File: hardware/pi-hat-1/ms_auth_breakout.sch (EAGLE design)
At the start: 37 parts, among them IC1 ULN2003AD, J11 BUCK_MODULEHORIZONTAL, J9 POWER_JACKPTH_LOCK, Q1 DMN3023L, Q2 DMN3023L, Q3 DMN3023L, Q4 DMN3023L, Q5 DMN3023L, Q6 DMN3023L

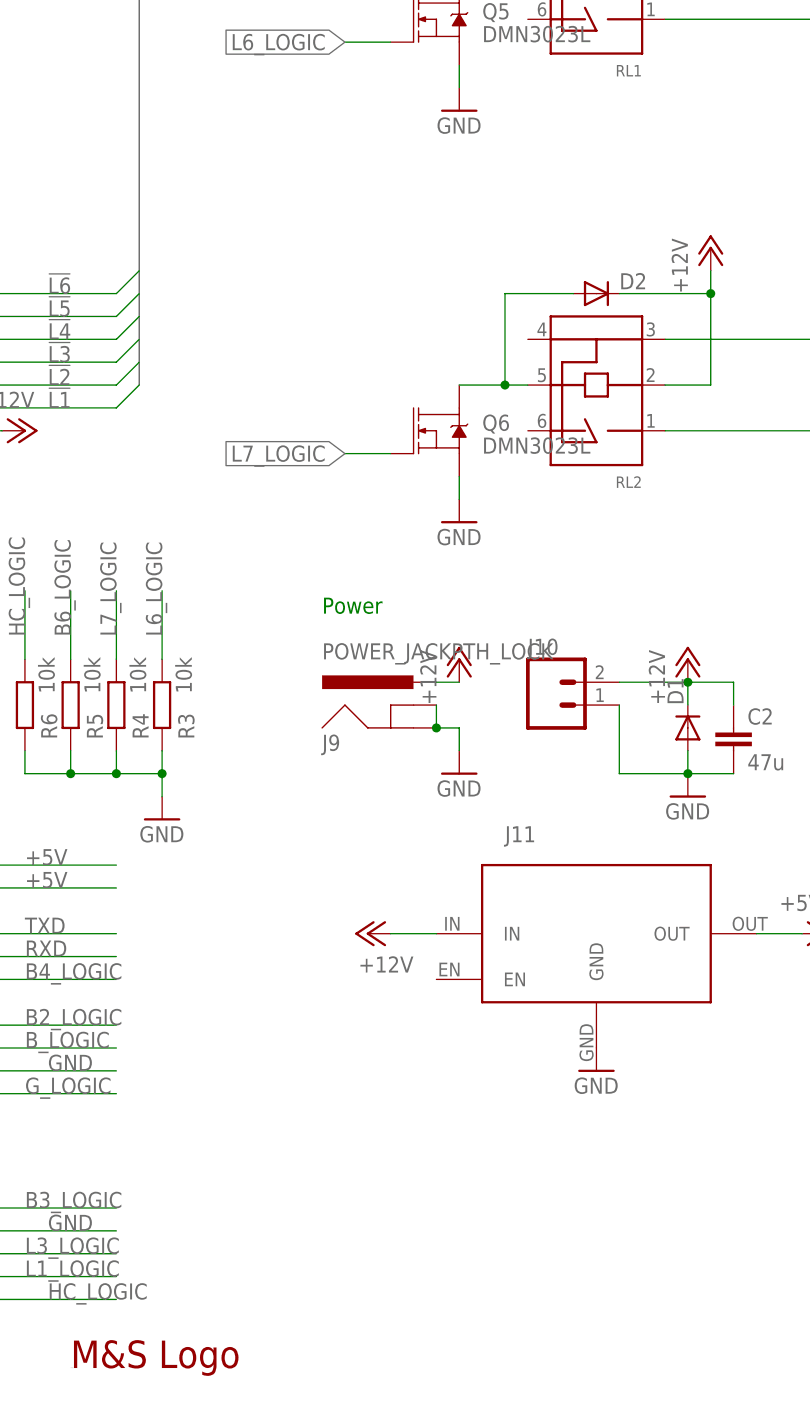
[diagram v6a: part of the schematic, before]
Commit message: Add relay MPN, OSH Certification mark
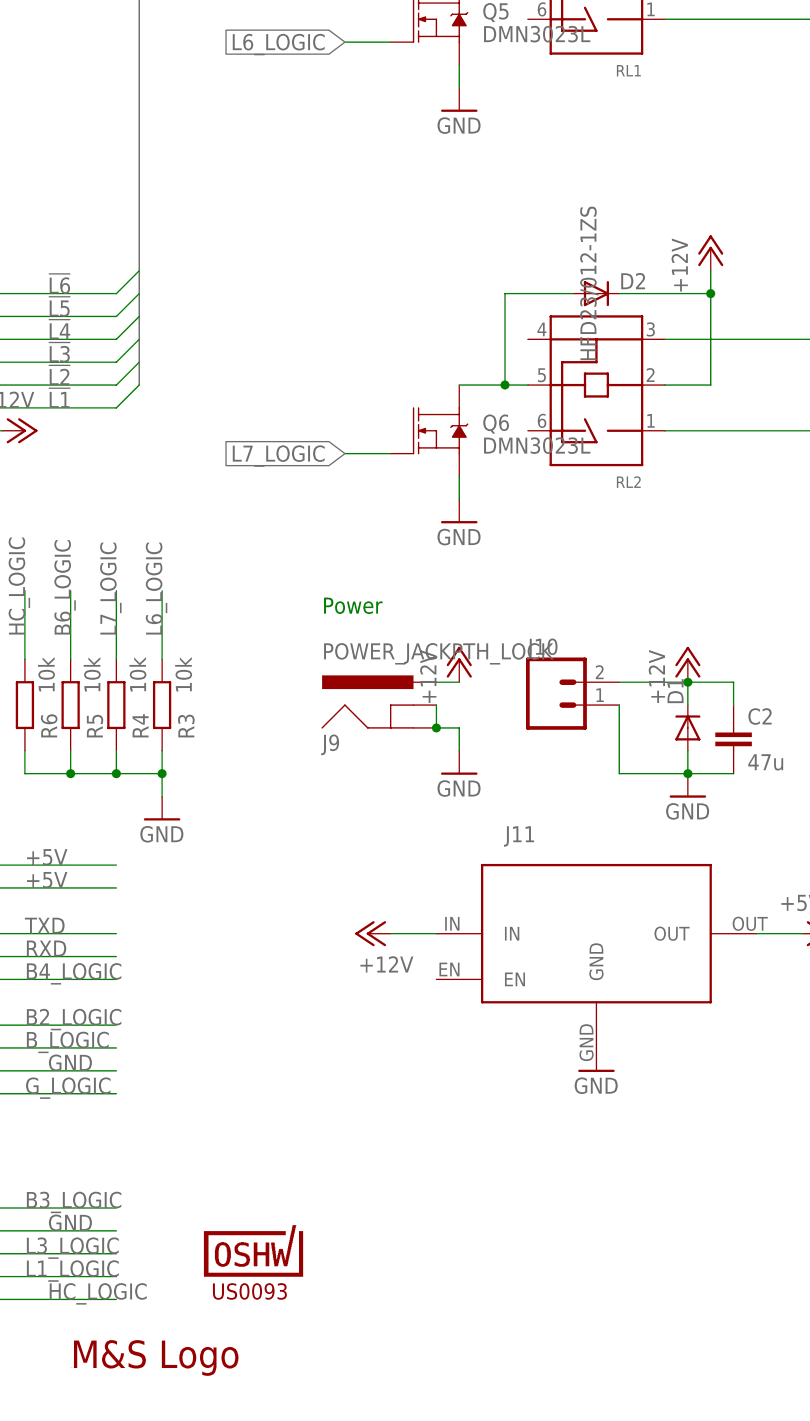
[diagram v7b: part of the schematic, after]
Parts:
- added U$2: US0093, OSHWA:CERT-SMALL
- RL1, RL2: MFN (none) -> HF; MPN (none) -> HFD23/012-1ZS
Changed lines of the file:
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@@
 <part name="Q5" library="SparkFun-DiscreteSemi" deviceset="MOSFET-NCH" device="-AO3404A" value="DMN3023L"/>
 <part name="Q6" library="SparkFun-DiscreteSemi" deviceset="MOSFET-NCH" device="-AO3404A" value="DMN3023L"/>
-<part name="RL1" library="hfd23" deviceset="HFD23_SPDT" device=""/>
-<part name="RL2" library="hfd23" deviceset="HFD23_SPDT" device=""/>
+<part name="RL1" library="hfd23" deviceset="HFD23_SPDT" device="">
+<attribute name="MFN" value="HF"/>
+<attribute name="MPN" value="HFD23/012-1ZS"/>
+</part>
+<part name="RL2" library="hfd23" deviceset="HFD23_SPDT" device="">
+<attribute name="MFN" value="HF"/>
+<attribute name="MPN" value="HFD23/012-1ZS"/>
+</part>
 <part name="GND9" library="supply1" deviceset="GND" device=""/>
 <part name="GND14" library="supply1" deviceset="GND" device=""/>
@@
 <part name="R6" library="Tim-Pretty" deviceset="R-EU_" device="R0805" value="10k"/>
 <part name="J5" library="SparkFun-Connectors" deviceset="CONN_06" device="POLAR_LOCK"/>
+<part name="U$2" library="OSHWA" deviceset="CERT" device="-SMALL" value="US0093"/>
 </parts>
 <sheets>
@@
 <instance part="Q5" gate="NMOS" x="157.48" y="157.48"/>
 <instance part="Q6" gate="NMOS" x="157.48" y="111.76"/>
-<instance part="RL1" gate="G$1" x="175.26" y="165.1" rot="R90"/>
-<instance part="RL2" gate="G$1" x="175.26" y="119.38" rot="R90"/>
+<instance part="RL1" gate="G$1" x="175.26" y="165.1" rot="R90">
+<attribute name="MFN" x="175.26" y="165.1" size="1.778" layer="96" rot="R90" display="off"/>
+<attribute name="MPN" x="175.26" y="165.1" size="1.778" layer="96" rot="R90" display="off"/>
+</instance>
+<instance part="RL2" gate="G$1" x="175.26" y="119.38" rot="R90">
+<attribute name="MFN" x="175.26" y="119.38" size="1.778" layer="96" rot="R90" display="off"/>
+<attribute name="MPN" x="175.26" y="119.38" size="1.778" layer="96" rot="R90"/>
+</instance>
 <instance part="GND9" gate="1" x="160.02" y="147.32"/>
 <instance part="GND14" gate="1" x="160.02" y="101.6"/>
@@
 </instance>
 <instance part="J5" gate="G$1" x="22.86" y="68.58"/>
+<instance part="U$2" gate="G$1" x="137.16" y="17.78"/>
 </instances>
 <busses>
